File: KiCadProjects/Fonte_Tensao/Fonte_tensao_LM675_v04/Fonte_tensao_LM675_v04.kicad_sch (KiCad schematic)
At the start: 30 parts, among them J1 Barrel_Jack, J2 sinais analogicos, J3 comunicacao / sinais digitais, J4 tensoes, U1 L7809, U2 LM7909_TO220, U3 LM675, U4 L7805, U5 L7905, U6 LM1117T-3.3

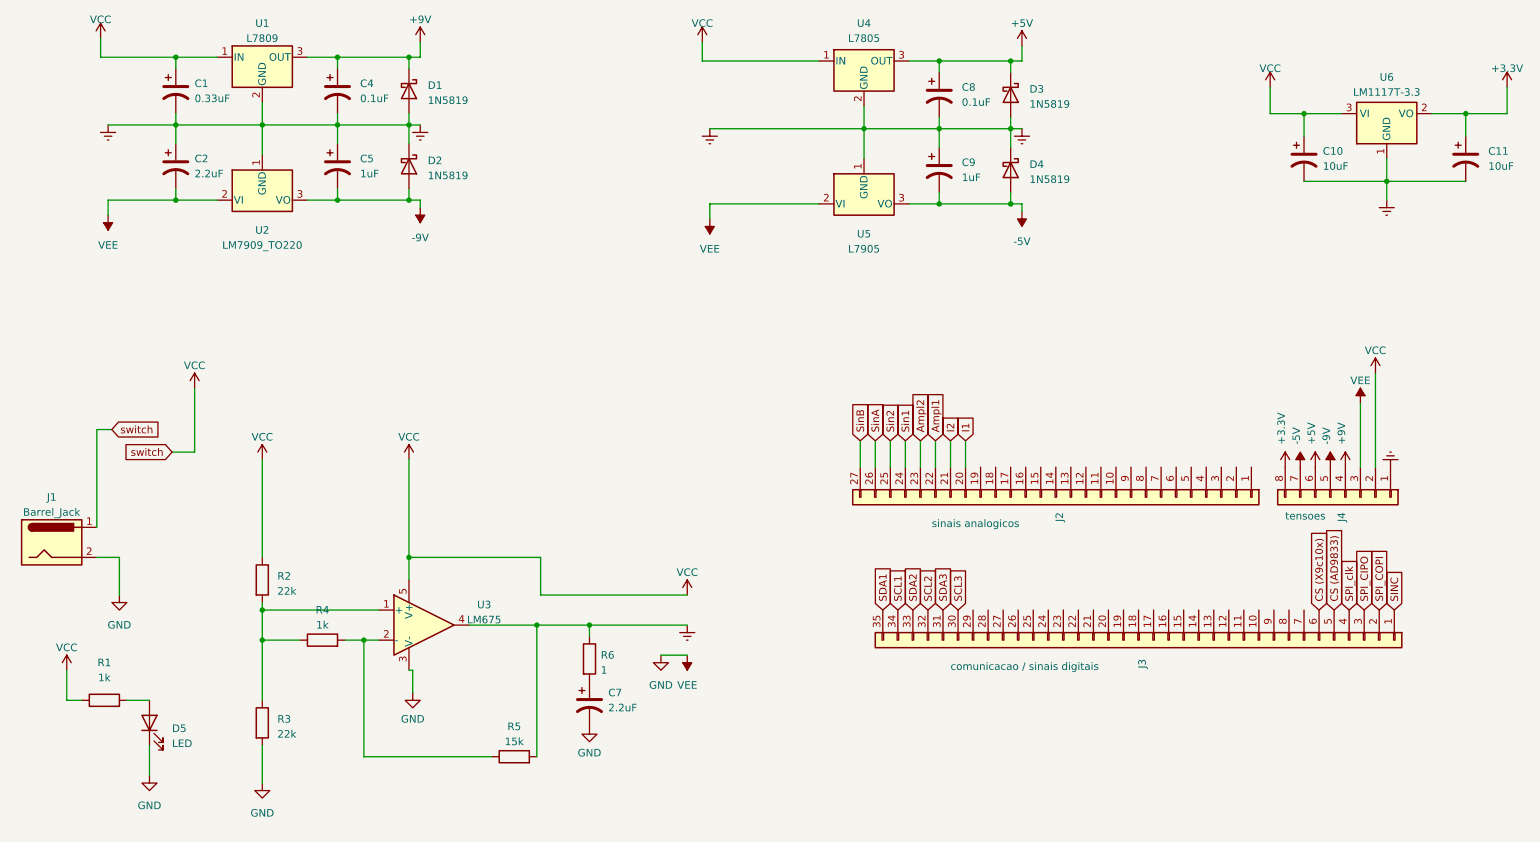
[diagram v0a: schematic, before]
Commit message: revisao de  v03 para os componentes utilizados no primeiro  prototipo
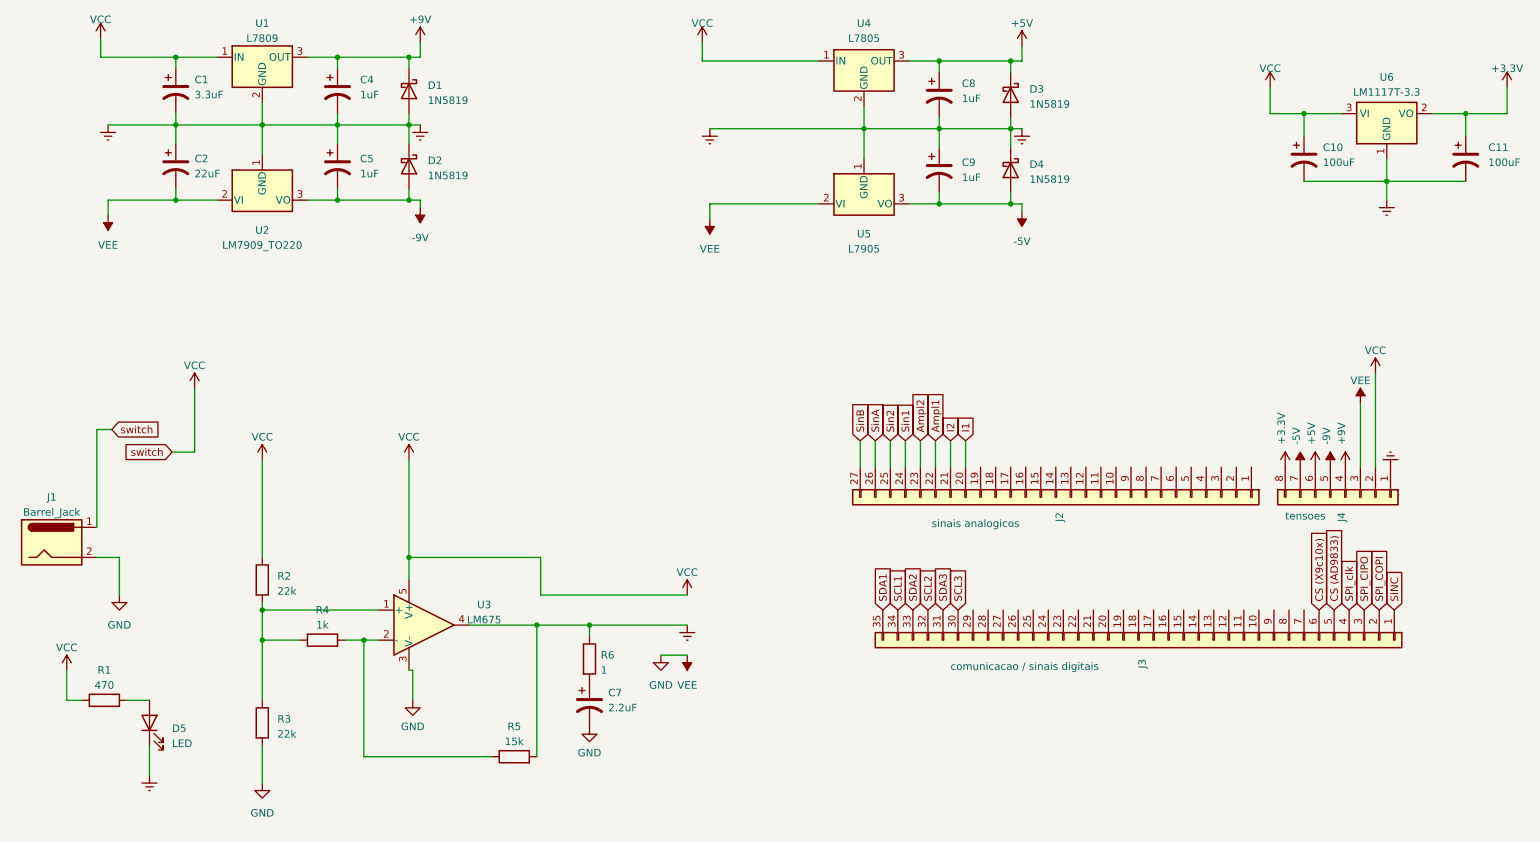
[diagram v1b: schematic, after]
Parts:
- C1: value 0.33uF -> 3.3uF
- C10, C11: value 10uF -> 100uF
- C2: value 2.2uF -> 22uF
- C4, C8: value 0.1uF -> 1uF
- R1: value 1k -> 470
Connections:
- net Earth: now also D5.1 (K)
- net GND: no longer D5.1 (K)

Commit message: Fonte de tensao v04 - Para fabricacao do segundo prototipo
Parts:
- R1, R2, R3, R4, R5, R6: footprint Resistor_THT:R_Axial_DIN0617_L17.0mm_D6.0mm_P20.32mm_Horizontal -> Resistor_THT:R_Axial_DIN0207_L6.3mm_D2.5mm_P7.62mm_Horizontal
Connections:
- net GND renamed VEE
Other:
- moved on the sheet: C7, R2, R3, R4, R5, R6, U3
